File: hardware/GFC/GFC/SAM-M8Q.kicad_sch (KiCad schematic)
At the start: 4 parts

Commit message: Some hardware changes, started to add footprints and part links to digikey. Switching most to SMD
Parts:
- C17: renamed from C?; footprint (none) -> Capacitor_SMD:C_0603_1608Metric_Pad1.08x0.95mm_HandSolder; Digikey (none) -> https://www.digikey.com/short/3wn2fdb2; Unit Price (none) -> 0.10
- U4: renamed from U?; Digikey (none) -> https://www.digikey.com/short/n7wwdb37; Unit Price (none) -> 31.50
- gave numbers to parts that had none: 2
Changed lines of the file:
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@@
   (symbol (lib_id "Device:C") (at 123.19 63.5 90) (unit 1)
     (in_bom yes) (on_board yes) (fields_autoplaced)
-    (property "Reference" "C?" (id 0) (at 123.19 55.88 90))
+    (property "Reference" "C17" (id 0) (at 123.19 55.88 90))
     (property "Value" "0.1uF" (id 1) (at 123.19 58.42 90))
-    (property "Footprint" "" (id 2) (at 127 62.5348 0)
+    (property "Footprint" "Capacitor_SMD:C_0603_1608Metric_Pad1.08x0.95mm_HandSolder" (id 2) (at 127 62.5348 0)
       (effects (font (size 1.27 1.27)) hide)
     )
     (property "Datasheet" "~" (id 3) (at 123.19 63.5 0)
+      (effects (font (size 1.27 1.27)) hide)
+    )
+    (property "Digikey" "https://www.digikey.com/short/3wn2fdb2" (id 4) (at 123.19 63.5 0)
+      (effects (font (size 1.27 1.27)) hide)
+    )
+    (property "Unit Price" "0.10" (id 5) (at 123.19 63.5 0)
       (effects (font (size 1.27 1.27)) hide)
     )
@@
   (symbol (lib_id "Device:FerriteBead") (at 156.21 87.63 90) (unit 1)
     (in_bom yes) (on_board yes) (fields_autoplaced)
-    (property "Reference" "FB?" (id 0) (at 156.1592 80.01 90))
+    (property "Reference" "FB1" (id 0) (at 156.1592 80.01 90))
     (property "Value" "FerriteBead" (id 1) (at 156.1592 82.55 90))
     (property "Footprint" "" (id 2) (at 156.21 89.408 90)
@@
   (symbol (lib_id "power:GND") (at 116.84 66.04 0) (unit 1)
     (in_bom yes) (on_board yes) (fields_autoplaced)
-    (property "Reference" "#PWR?" (id 0) (at 116.84 72.39 0)
+    (property "Reference" "#PWR0149" (id 0) (at 116.84 72.39 0)
       (effects (font (size 1.27 1.27)) hide)
     )
@@
   (symbol (lib_id "Device:FerriteBead") (at 156.21 93.98 270) (unit 1)
     (in_bom yes) (on_board yes)
-    (property "Reference" "FB?" (id 0) (at 156.21 97.79 90))
+    (property "Reference" "FB2" (id 0) (at 156.21 97.79 90))
     (property "Value" "FerriteBead" (id 1) (at 156.21 100.33 90))
     (property "Footprint" "" (id 2) (at 156.21 92.202 90)
@@
   (symbol (lib_id "RF_GPS:SAM-M8Q") (at 133.35 87.63 0) (unit 1)
     (in_bom yes) (on_board yes) (fields_autoplaced)
-    (property "Reference" "U?" (id 0) (at 135.3694 100.33 0)
+    (property "Reference" "U4" (id 0) (at 135.3694 100.33 0)
       (effects (font (size 1.27 1.27)) (justify left))
     )
@@
     )
     (property "Datasheet" "https://www.u-blox.com/sites/default/files/SAM-M8Q_DataSheet_%28UBX-16012619%29.pdf" (id 3) (at 133.35 87.63 0)
+      (effects (font (size 1.27 1.27)) hide)
+    )
+    (property "Digikey" "https://www.digikey.com/short/n7wwdb37" (id 4) (at 133.35 87.63 0)
+      (effects (font (size 1.27 1.27)) hide)
+    )
+    (property "Unit Price" "31.50" (id 5) (at 133.35 87.63 0)
       (effects (font (size 1.27 1.27)) hide)
     )
@@
   (symbol (lib_id "power:GND") (at 133.35 104.14 0) (unit 1)
     (in_bom yes) (on_board yes) (fields_autoplaced)
-    (property "Reference" "#PWR?" (id 0) (at 133.35 110.49 0)
+    (property "Reference" "#PWR0150" (id 0) (at 133.35 110.49 0)
       (effects (font (size 1.27 1.27)) hide)
     )

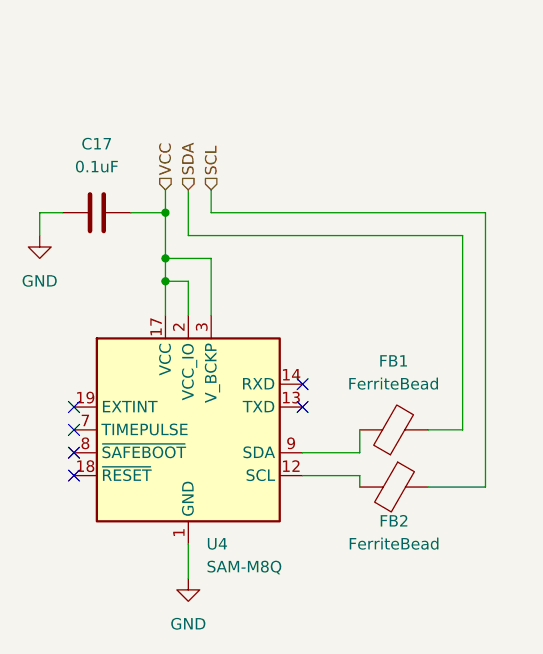
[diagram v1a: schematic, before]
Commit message: Updated footprints - Started work on PCB layout
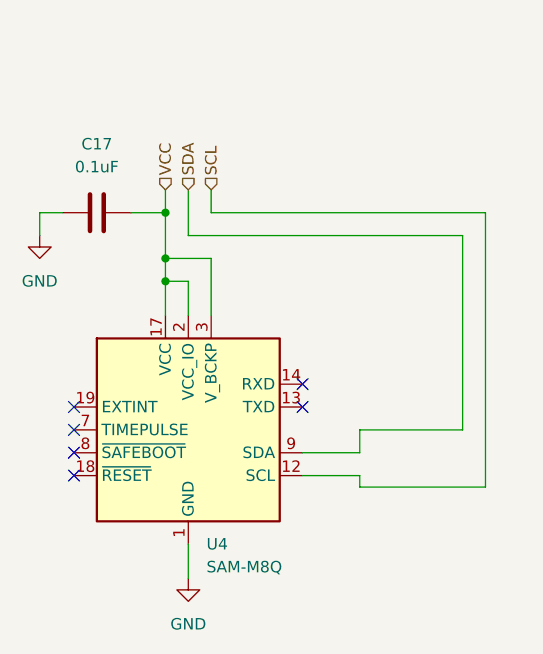
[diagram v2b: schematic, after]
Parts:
- removed FB1, FB2: FerriteBead, symbol Device:FerriteBead
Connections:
- net SCL: now also U4.12 (SCL)
- net SDA: now also U4.9 (SDA)
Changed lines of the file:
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@@
   (no_connect (at 146.05 85.09))
   (no_connect (at 120.65 85.09))
-  (wire (pts (xy 160.02 93.98) (xy 166.37 93.98))
+  (wire (pts (xy 152.4 93.98) (xy 166.37 93.98))
     (stroke (width 0) (type default) (color 0 0 0 0))
   )
@@
     (stroke (width 0) (type default) (color 0 0 0 0))
   )
-  (wire (pts (xy 160.02 87.63) (xy 163.83 87.63))
+  (wire (pts (xy 152.4 87.63) (xy 163.83 87.63))
     (stroke (width 0) (type default) (color 0 0 0 0))
   )
@@
     (pin "2")
   )
-  (symbol (lib_id "Device:FerriteBead") (at 156.21 87.63 90) (unit 1)
-    (in_bom yes) (on_board yes) (fields_autoplaced)
-    (property "Reference" "FB1" (id 0) (at 156.1592 80.01 90))
-    (property "Value" "FerriteBead" (id 1) (at 156.1592 82.55 90))
-    (property "Footprint" "" (id 2) (at 156.21 89.408 90)
-      (effects (font (size 1.27 1.27)) hide)
-    )
-    (property "Datasheet" "~" (id 3) (at 156.21 87.63 0)
-      (effects (font (size 1.27 1.27)) hide)
-    )
-    (pin "1")
-    (pin "2")
-  )
   (symbol (lib_id "power:GND") (at 116.84 66.04 0) (unit 1)
     (in_bom yes) (on_board yes) (fields_autoplaced)
@@
     (pin "1")
   )
-  (symbol (lib_id "Device:FerriteBead") (at 156.21 93.98 270) (unit 1)
-    (in_bom yes) (on_board yes)
-    (property "Reference" "FB2" (id 0) (at 156.21 97.79 90))
-    (property "Value" "FerriteBead" (id 1) (at 156.21 100.33 90))
-    (property "Footprint" "" (id 2) (at 156.21 92.202 90)
-      (effects (font (size 1.27 1.27)) hide)
-    )
-    (property "Datasheet" "~" (id 3) (at 156.21 93.98 0)
-      (effects (font (size 1.27 1.27)) hide)
-    )
-    (pin "1")
-    (pin "2")
-  )
   (symbol (lib_id "RF_GPS:SAM-M8Q") (at 133.35 87.63 0) (unit 1)

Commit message: Schematic Update - ADC/DAC & GPIO Config EEPROM
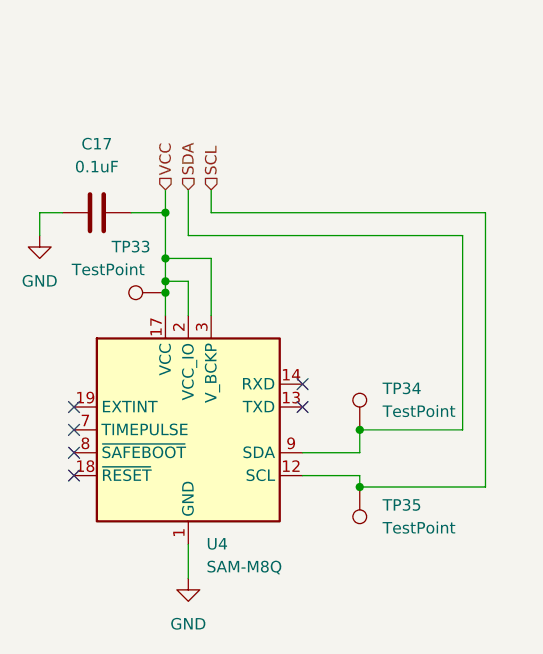
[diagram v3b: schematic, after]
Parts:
- added TP33, TP34, TP35: TestPoint, TestPoint:TestPoint_Pad_D1.0mm, symbol Connector:TestPoint
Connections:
- net SCL: now also TP35.1
- net SDA: now also TP34.1
- net VCC: now also TP33.1
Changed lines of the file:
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@@
   (junction (at 130.81 68.58) (diameter 0) (color 0 0 0 0)
   )
+  (junction (at 152.4 87.63) (diameter 0) (color 0 0 0 0)
+  )
   (junction (at 130.81 71.12) (diameter 0) (color 0 0 0 0)
+  )
+  (junction (at 130.81 72.39) (diameter 0) (color 0 0 0 0)
+  )
+  (junction (at 152.4 93.98) (diameter 0) (color 0 0 0 0)
   )
   (no_connect (at 120.65 92.71))
@@
     (stroke (width 0) (type default) (color 0 0 0 0))
   )
-  (wire (pts (xy 130.81 71.12) (xy 130.81 74.93))
+  (wire (pts (xy 130.81 71.12) (xy 130.81 72.39))
     (stroke (width 0) (type default) (color 0 0 0 0))
   )
@@
   )
   (wire (pts (xy 152.4 92.71) (xy 152.4 93.98))
+    (stroke (width 0) (type default) (color 0 0 0 0))
+  )
+  (wire (pts (xy 130.81 72.39) (xy 130.81 74.93))
     (stroke (width 0) (type default) (color 0 0 0 0))
   )
@@
     (effects (font (size 1.27 1.27)) (justify left))
   )
+  (symbol (lib_id "Connector:TestPoint") (at 152.4 87.63 0) (unit 1)
+    (in_bom yes) (on_board yes) (fields_autoplaced)
+    (property "Reference" "TP34" (id 0) (at 154.94 83.0579 0)
+      (effects (font (size 1.27 1.27)) (justify left))
+    )
+    (property "Value" "TestPoint" (id 1) (at 154.94 85.5979 0)
+      (effects (font (size 1.27 1.27)) (justify left))
+    )
+    (property "Footprint" "TestPoint:TestPoint_Pad_D1.0mm" (id 2) (at 157.48 87.63 0)
+      (effects (font (size 1.27 1.27)) hide)
+    )
+    (property "Datasheet" "~" (id 3) (at 157.48 87.63 0)
+      (effects (font (size 1.27 1.27)) hide)
+    )
+    (pin "1")
+  )
   (symbol (lib_id "Device:C") (at 123.19 63.5 90) (unit 1)
     (in_bom yes) (on_board yes) (fields_autoplaced)
@@
     (pin "2")
   )
+  (symbol (lib_id "Connector:TestPoint") (at 130.81 72.39 90) (unit 1)
+    (in_bom yes) (on_board yes)
+    (property "Reference" "TP33" (id 0) (at 127 67.31 90))
+    (property "Value" "TestPoint" (id 1) (at 124.46 69.85 90))
+    (property "Footprint" "TestPoint:TestPoint_Pad_D1.0mm" (id 2) (at 130.81 67.31 0)
+      (effects (font (size 1.27 1.27)) hide)
+    )
+    (property "Datasheet" "~" (id 3) (at 130.81 67.31 0)
+      (effects (font (size 1.27 1.27)) hide)
+    )
+    (pin "1")
+  )
   (symbol (lib_id "power:GND") (at 116.84 66.04 0) (unit 1)
     (in_bom yes) (on_board yes) (fields_autoplaced)
@@
       (effects (font (size 1.27 1.27)) hide)
     )
+    (pin "1")
+  )
+  (symbol (lib_id "Connector:TestPoint") (at 152.4 93.98 180) (unit 1)
+    (in_bom yes) (on_board yes) (fields_autoplaced)
+    (property "Reference" "TP35" (id 0) (at 154.94 96.0119 0)
+      (effects (font (size 1.27 1.27)) (justify right))
+    )
+    (property "Value" "TestPoint" (id 1) (at 154.94 98.5519 0)
+      (effects (font (size 1.27 1.27)) (justify right))
+    )
+    (property "Footprint" "TestPoint:TestPoint_Pad_D1.0mm" (id 2) (at 147.32 93.98 0)
+      (effects (font (size 1.27 1.27)) hide)
+    )
+    (property "Datasheet" "~" (id 3) (at 147.32 93.98 0)
+      (effects (font (size 1.27 1.27)) hide)
+    )

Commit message: sync
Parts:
- removed TP33, TP34, TP35: TestPoint, TestPoint:TestPoint_Pad_D1.0mm, symbol Connector:TestPoint
- added TP42, TP43: Test Point, TestPoint:TestPoint_Pad_D1.0mm, symbol Connector:TestPoint_Small
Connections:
- net SCL renamed I2C0.SCL
- net I2C0.SCL: now also TP43.1
- net SDA renamed I2C0.SDA
- net I2C0.SDA: now also TP42.1
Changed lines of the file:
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@@
   (junction (at 130.81 63.5) (diameter 0) (color 0 0 0 0)
+  )
+  (junction (at 147.3561 92.71) (diameter 0) (color 0 0 0 0)
   )
   (junction (at 130.81 68.58) (diameter 0) (color 0 0 0 0)
   )
-  (junction (at 152.4 87.63) (diameter 0) (color 0 0 0 0)
+  (junction (at 147.32 90.17) (diameter 0) (color 0 0 0 0)
   )
   (junction (at 130.81 71.12) (diameter 0) (color 0 0 0 0)
-  )
-  (junction (at 130.81 72.39) (diameter 0) (color 0 0 0 0)
-  )
-  (junction (at 152.4 93.98) (diameter 0) (color 0 0 0 0)
   )
   (no_connect (at 120.65 92.71))
@@
   (no_connect (at 146.05 85.09))
   (no_connect (at 120.65 85.09))
+  (bus_entry (at 151.13 43.18) (size -2.54 2.54)
+    (stroke (width 0) (type default) (color 0 0 0 0))
+  )
+  (bus_entry (at 151.13 46.99) (size -2.54 2.54)
+    (stroke (width 0) (type default) (color 0 0 0 0))
+  )
   (wire (pts (xy 152.4 93.98) (xy 166.37 93.98))
     (stroke (width 0) (type default) (color 0 0 0 0))
   )
-  (wire (pts (xy 133.35 66.04) (xy 133.35 60.96))
+  (wire (pts (xy 146.05 90.17) (xy 147.32 90.17))
     (stroke (width 0) (type default) (color 0 0 0 0))
   )
-  (wire (pts (xy 146.05 90.17) (xy 152.4 90.17))
+  (bus (pts (xy 152.4 43.18) (xy 151.13 43.18))
     (stroke (width 0) (type default) (color 0 0 0 0))
   )
-  (wire (pts (xy 130.81 71.12) (xy 130.81 72.39))
+  (wire (pts (xy 130.81 71.12) (xy 130.81 74.93))
     (stroke (width 0) (type default) (color 0 0 0 0))
   )
@@
   )
   (wire (pts (xy 166.37 63.5) (xy 135.89 63.5))
+    (stroke (width 0) (type default) (color 0 0 0 0))
+  )
+  (wire (pts (xy 148.59 45.72) (xy 133.35 45.72))
     (stroke (width 0) (type default) (color 0 0 0 0))
   )
@@
     (stroke (width 0) (type default) (color 0 0 0 0))
   )
-  (wire (pts (xy 130.81 72.39) (xy 130.81 74.93))
-    (stroke (width 0) (type default) (color 0 0 0 0))
-  )
   (wire (pts (xy 130.81 68.58) (xy 130.81 71.12))
     (stroke (width 0) (type default) (color 0 0 0 0))
@@
     (stroke (width 0) (type default) (color 0 0 0 0))
   )
-  (wire (pts (xy 146.05 92.71) (xy 152.4 92.71))
+  (wire (pts (xy 146.05 92.71) (xy 147.3561 92.71))
+    (stroke (width 0) (type default) (color 0 0 0 0))
+  )
+  (wire (pts (xy 147.32 90.17) (xy 152.4 90.17))
     (stroke (width 0) (type default) (color 0 0 0 0))
   )
   (wire (pts (xy 130.81 60.96) (xy 130.81 63.5))
+    (stroke (width 0) (type default) (color 0 0 0 0))
+  )
+  (bus (pts (xy 151.13 43.18) (xy 151.13 46.99))
+    (stroke (width 0) (type default) (color 0 0 0 0))
+  )
+  (wire (pts (xy 147.3561 92.71) (xy 152.4 92.71))
     (stroke (width 0) (type default) (color 0 0 0 0))
   )
@@
   )
   (wire (pts (xy 130.81 63.5) (xy 130.81 68.58))
+    (stroke (width 0) (type default) (color 0 0 0 0))
+  )
+  (wire (pts (xy 135.89 49.53) (xy 148.59 49.53))
     (stroke (width 0) (type default) (color 0 0 0 0))
   )
@@
     (stroke (width 0) (type default) (color 0 0 0 0))
   )
-  (wire (pts (xy 135.89 63.5) (xy 135.89 60.96))
+  (wire (pts (xy 135.89 49.53) (xy 135.89 63.5))
     (stroke (width 0) (type default) (color 0 0 0 0))
   )
@@
     (stroke (width 0) (type default) (color 0 0 0 0))
   )
-  (hierarchical_label "SCL" (shape input) (at 135.89 60.96 90)
-    (effects (font (size 1.27 1.27)) (justify left))
+  (wire (pts (xy 133.35 45.72) (xy 133.35 66.04))
+    (stroke (width 0) (type default) (color 0 0 0 0))
   )
-  (hierarchical_label "SDA" (shape input) (at 133.35 60.96 90)
+  (label "I2C0.SDA" (at 139.7 45.72 0)
+    (effects (font (size 1.27 1.27)) (justify left bottom))
+  )
+  (label "I2C0.SCL" (at 139.7 49.53 0)
+    (effects (font (size 1.27 1.27)) (justify left bottom))
+  )
+  (hierarchical_label "I2C0{SDA SCL}" (shape input) (at 152.4 43.18 0)
     (effects (font (size 1.27 1.27)) (justify left))
   )
@@
     (effects (font (size 1.27 1.27)) (justify left))
   )
-  (symbol (lib_id "Connector:TestPoint") (at 152.4 87.63 0) (unit 1)
-    (in_bom yes) (on_board yes) (fields_autoplaced)
-    (property "Reference" "TP34" (id 0) (at 154.94 83.0579 0)
+  (symbol (lib_id "Connector:TestPoint_Small") (at 147.3561 92.71 0) (mirror y) (unit 1)
+    (in_bom yes) (on_board yes)
+    (property "Reference" "TP43" (id 0) (at 151.1661 91.44 0)
       (effects (font (size 1.27 1.27)) (justify left))
     )
-    (property "Value" "TestPoint" (id 1) (at 154.94 85.5979 0)
-      (effects (font (size 1.27 1.27)) (justify left))
+    (property "Value" "Test Point" (id 1) (at 146.0861 93.9799 0)
+      (effects (font (size 1.27 1.27)) (justify left) hide)
     )
-    (property "Footprint" "TestPoint:TestPoint_Pad_D1.0mm" (id 2) (at 157.48 87.63 0)
+    (property "Footprint" "TestPoint:TestPoint_Pad_D1.0mm" (id 2) (at 142.2761 92.71 0)
       (effects (font (size 1.27 1.27)) hide)
     )
-    (property "Datasheet" "~" (id 3) (at 157.48 87.63 0)
+    (property "Datasheet" "~" (id 3) (at 142.2761 92.71 0)
       (effects (font (size 1.27 1.27)) hide)
     )
@@
     (pin "2")
   )
-  (symbol (lib_id "Connector:TestPoint") (at 130.81 72.39 90) (unit 1)
+  (symbol (lib_id "Connector:TestPoint_Small") (at 147.32 90.17 0) (mirror y) (unit 1)
     (in_bom yes) (on_board yes)
-    (property "Reference" "TP33" (id 0) (at 127 67.31 90))
-    (property "Value" "TestPoint" (id 1) (at 124.46 69.85 90))
-    (property "Footprint" "TestPoint:TestPoint_Pad_D1.0mm" (id 2) (at 130.81 67.31 0)
+    (property "Reference" "TP42" (id 0) (at 151.13 88.9 0)
+      (effects (font (size 1.27 1.27)) (justify left))
+    )
+    (property "Value" "Test Point" (id 1) (at 146.05 91.4399 0)
+      (effects (font (size 1.27 1.27)) (justify left) hide)
+    )
+    (property "Footprint" "TestPoint:TestPoint_Pad_D1.0mm" (id 2) (at 142.24 90.17 0)
       (effects (font (size 1.27 1.27)) hide)
     )
-    (property "Datasheet" "~" (id 3) (at 130.81 67.31 0)
+    (property "Datasheet" "~" (id 3) (at 142.24 90.17 0)
       (effects (font (size 1.27 1.27)) hide)
     )
@@
       (effects (font (size 1.27 1.27)) hide)
     )
-    (pin "1")
-  )
-  (symbol (lib_id "Connector:TestPoint") (at 152.4 93.98 180) (unit 1)
-    (in_bom yes) (on_board yes) (fields_autoplaced)
-    (property "Reference" "TP35" (id 0) (at 154.94 96.0119 0)
-      (effects (font (size 1.27 1.27)) (justify right))
-    )
-    (property "Value" "TestPoint" (id 1) (at 154.94 98.5519 0)
-      (effects (font (size 1.27 1.27)) (justify right))
-    )
-    (property "Footprint" "TestPoint:TestPoint_Pad_D1.0mm" (id 2) (at 147.32 93.98 0)
-      (effects (font (size 1.27 1.27)) hide)
-    )
-    (property "Datasheet" "~" (id 3) (at 147.32 93.98 0)
-      (effects (font (size 1.27 1.27)) hide)
-    )
